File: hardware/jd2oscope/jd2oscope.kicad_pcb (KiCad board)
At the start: 4 copper layers, 83 x 120 mm, 61 parts, among them J1 9V_CONN, J2 CONBNC001, J3 CONBNC001, U1 ESP32-DEVKITC-32D, U2 ILI9341-320x240-TFT-Touch, U3 NCP1117-5.0_SOT223, U4 OPA192IDBVR, U5 ADS7279IPW, U6 OPA192IDBVR, U7 ADS7279IPW

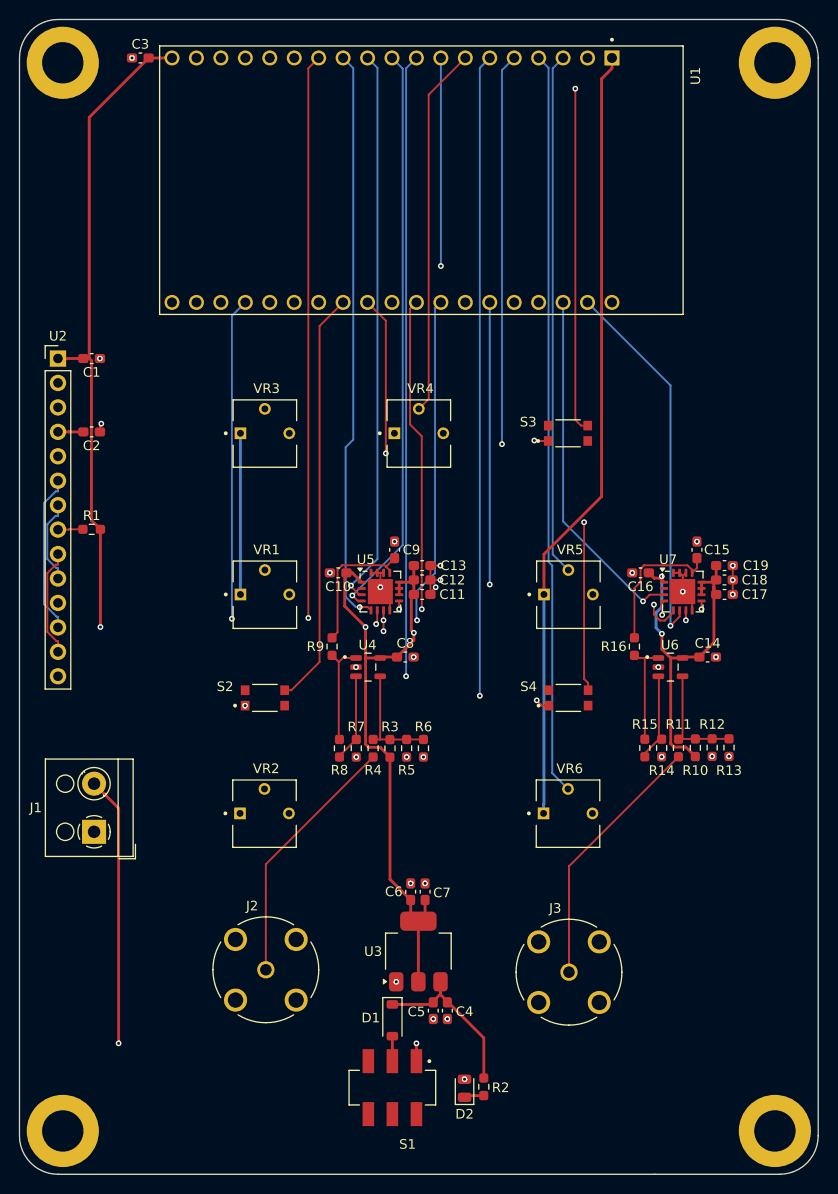
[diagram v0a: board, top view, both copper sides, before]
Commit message: fix: M4 -> M3 & re-exported 3d models
3d models now represent M3 board instead of M4 board (the mounting holes); I also added a cooler version with copper and vias, because well, it looks cooler (and also for "improved structural integrity) and whatnot when screwing stuffs in, too)
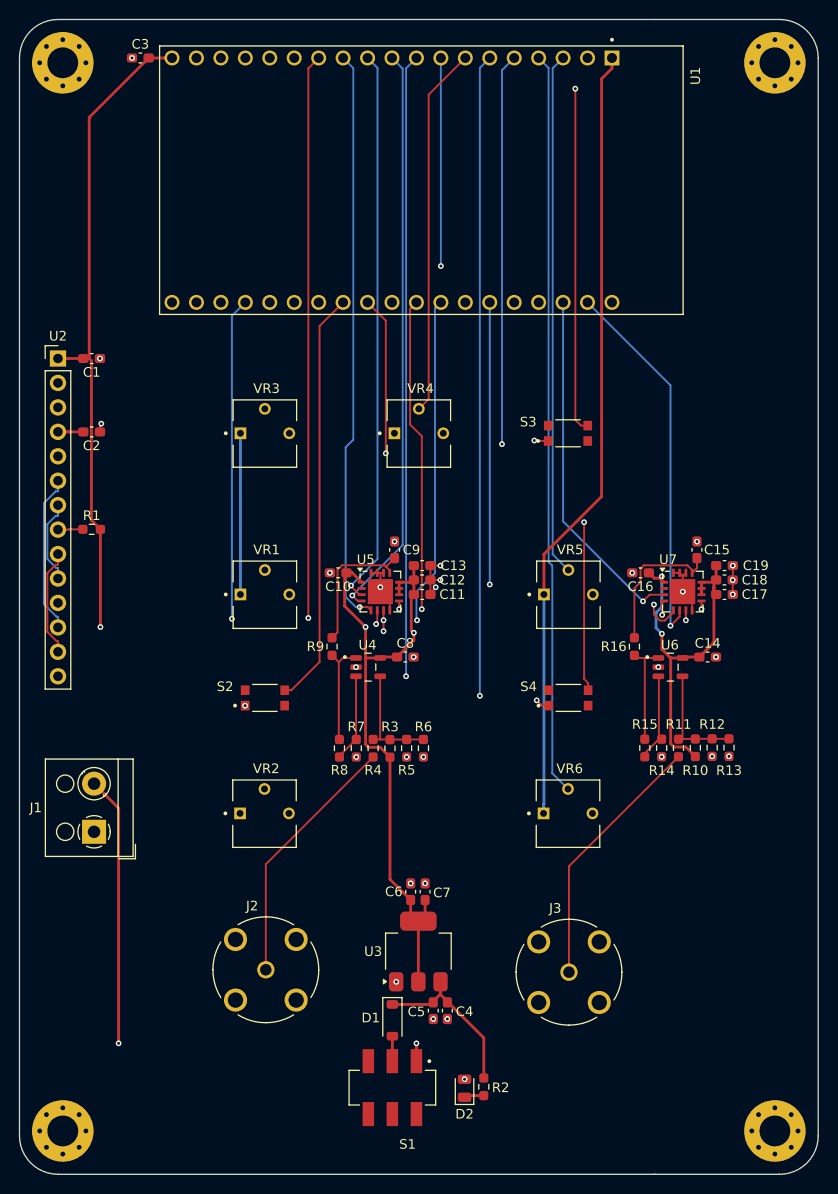
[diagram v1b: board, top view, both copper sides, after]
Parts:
- REF1, REF2, REF3, REF4: value MountingHole_4.3mm_M4_DIN965_Pad -> MountingHole_3.2mm_M3_Pad_Via; footprint MountingHole:MountingHole_4.3mm_M4_DIN965_Pad -> MountingHole:MountingHole_3.2mm_M3_Pad_Via
- moved REF1 74.0 mm to (106.8, 32.8)
- moved REF2 74.0 mm to (180.8, 32.8)
